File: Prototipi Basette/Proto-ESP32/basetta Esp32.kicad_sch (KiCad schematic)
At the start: 12 parts, among them J1 Conn_01x19, J2 Conn_01x19, J3 Conn_01x19, J4 Conn_01x19, J5 Screw_Terminal_01x02, J6 Conn_01x05, U1 L7805

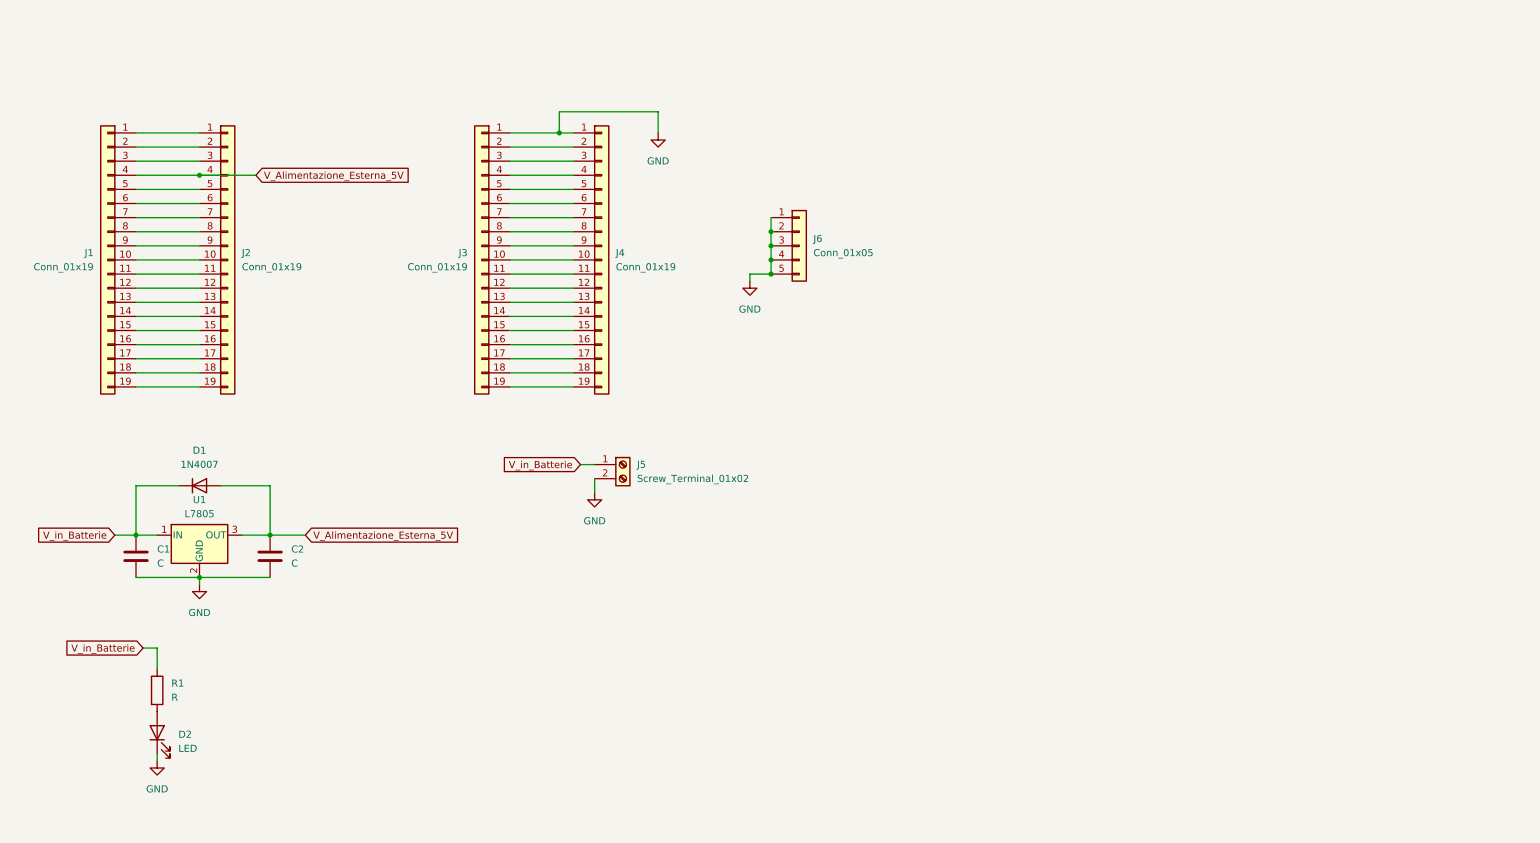
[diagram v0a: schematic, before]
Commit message: Add LM2596 symbol/footprint and update PCB
Add LM2596 footprint and symbol libraries, update project schematic and PCB files, and refresh project metadata. Includes new Library.pretty/LM2596 - IC footprint, Simboli_Progetto.* symbol library files, updated basetta Esp32.kicad_pcb/.kicad_sch/.kicad_pro/.kicad_prl and fp-info-cache, plus fp-lib-table and sym-lib-table. Several backup ZIPs were removed and replaced with new timestamped backups, and freerouting/temp freerouting files and a freerouting plugin ZIP were added.
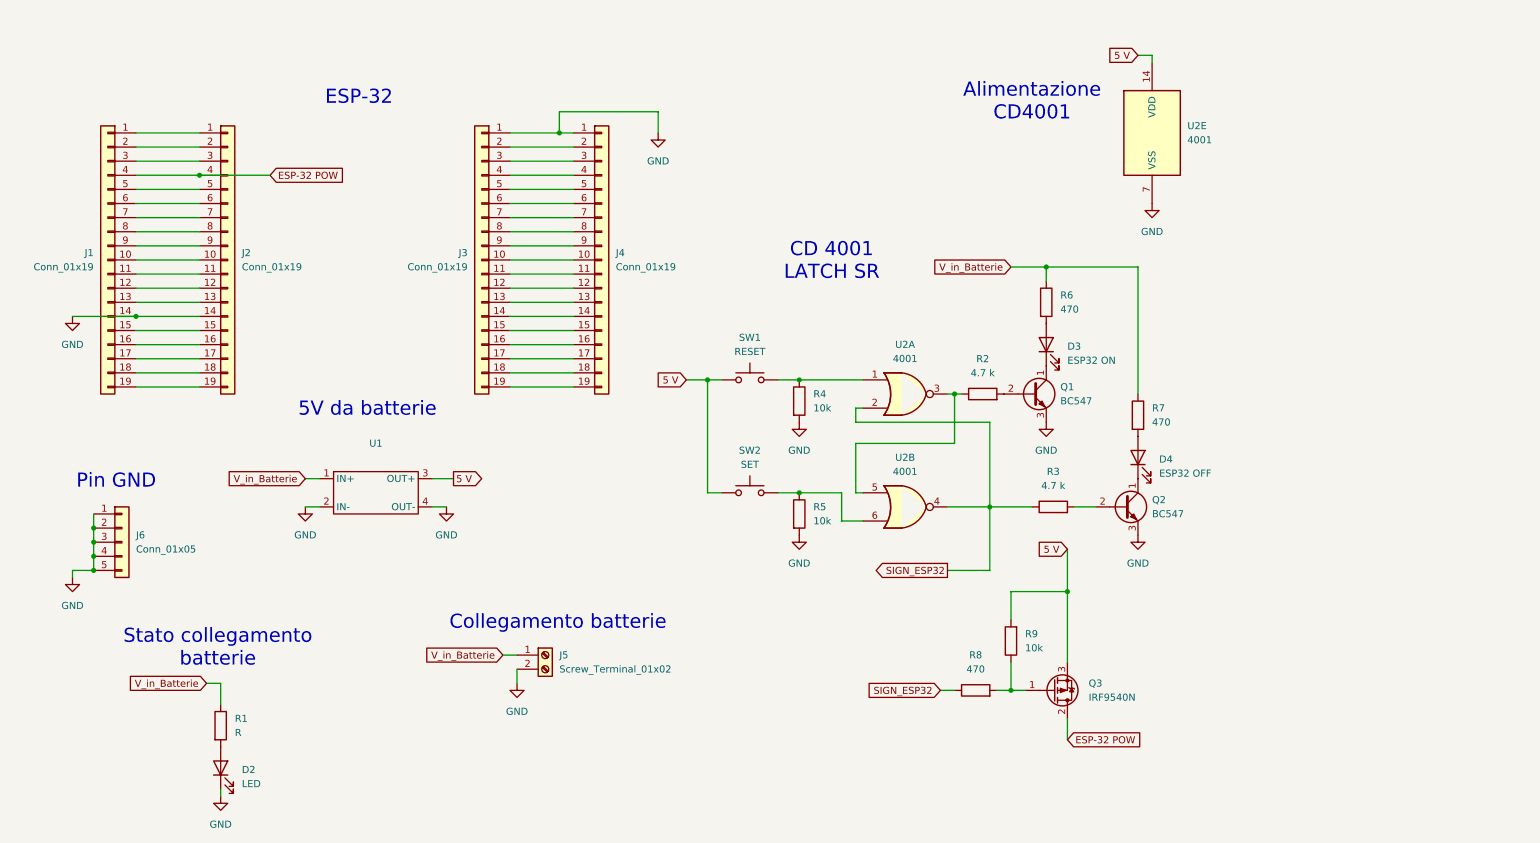
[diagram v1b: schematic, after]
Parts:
- removed C1: C, Capacitor_THT:C_Rect_L13.0mm_W5.0mm_P10.00mm_FKS3_FKP3_MKS4, symbol Device:C
- removed C2: C, Capacitor_THT:C_Disc_D5.0mm_W2.5mm_P5.00mm, symbol Device:C
- removed D1: 1N4007, Diode_THT:D_DO-41_SOD81_P7.62mm_Horizontal, symbol Diode:1N4007
- removed U1: L7805, Package_TO_SOT_THT:TO-220-3_Horizontal_TabUp, symbol Regulator_Linear:L7805
- added D3: ESP32 ON, LED_THT:LED_D5.0mm, symbol Device:LED
- added D4: ESP32 OFF, LED_THT:LED_D5.0mm, symbol Device:LED
- added Q1, Q2: BC547, Package_TO_SOT_THT:TO-92_Inline, symbol Transistor_BJT:BC547
- added Q3: IRF9540N, Package_TO_SOT_THT:TO-220-3_Vertical, symbol Transistor_FET:IRF9540N
- added R2, R3: 4.7 k, Resistor_THT:R_Axial_DIN0207_L6.3mm_D2.5mm_P7.62mm_Horizontal, symbol Device:R
- added R4, R5, R9: 10k, Resistor_THT:R_Axial_DIN0207_L6.3mm_D2.5mm_P7.62mm_Horizontal, symbol Device:R
- added R6, R7, R8: 470, Resistor_THT:R_Axial_DIN0207_L6.3mm_D2.5mm_P7.62mm_Horizontal, symbol Device:R
- added SW1: RESET, Button_Switch_THT:SW_PUSH_6mm_H4.3mm, symbol Switch:SW_Push
- added SW2: SET, Button_Switch_THT:SW_PUSH_6mm_H4.3mm, symbol Switch:SW_Push
- added U1: ~, Library:LM2596 - IC, symbol Simboli_Progetto:LM2596_IC
- added U2: 4001, Package_DIP:DIP-14_W7.62mm, symbol 4xxx:4001
- J5: footprint TerminalBlock:TerminalBlock_Altech_AK300-2_P5.00mm -> TerminalBlock:TerminalBlock_MaiXu_MX126-5.0-02P_1x02_P5.00mm
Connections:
- net GND: now also J1.14 (Pin_14), J2.14 (Pin_14), Q1.3 (E), Q2.3 (E), R4.2, R5.2, U1.2 (IN-), U1.4 (OUT-), U2.7 (VSS)
- net V_in_Batterie: now also R6.1, R7.1, U1.1 (IN+)
- net V_Alimentazione_Esterna_5V renamed ESP-32 POW
- net ESP-32 POW: now also Q3.2 (D)
- new net: R5.1, SW2.2, U2.6
- new net: Q2.2 (B), R3.2
- new net: D4.1 (K), Q2.1 (C)
- new net: Q3.1 (G), R8.2, R9.1
- new net: D4.2 (A), R7.2
- new net: R2.1, U2.3, U2.5
- new net: Q1.2 (B), R2.2
- new net: D3.2 (A), R6.2
- new net: R4.1, SW1.2, U2.1
- new net: D3.1 (K), Q1.1 (C)
- new net 5 V: Q3.3 (S), R9.2, SW1.1, SW2.1, U1.3 (OUT+), U2.14 (VDD)
- new net SIGN_ESP32: R3.1, R8.1, U2.2, U2.4
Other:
- note added: "5V da batterie"
- note added: "Alimentazione CD4001"
- note added: "CD 4001 LATCH SR"
- note added: "Collegamento batterie"
- note added: "ESP-32"
- note added: "Pin GND"
- note added: "Stato collegamento batterie"
- company: (none) -> Prof. Bernardis Pierluigi
- title: (none) -> Proto ESP-32
- moved on the sheet: D2, J5, J6, R1

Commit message: Update ESP32 board files and docs
Add compiled Arduino/main.pdf and simplify Arduino/pulsante.tex (remove blocking debouncing example and tidy Bounce2 section). Add several timestamped basetta Esp32 backup ZIPs. Large KiCad changes to basetta Esp32: update .kicad_pcb footprints, pads, nets and 3D models (replace/adjust LED/resistor footprints, add 1x19 pin socket connector, LM2596 module, DIP U3 and many pads; adjust silk/fab layers, pad geometry and UUIDs), and update related project files (.kicad_sch, .kicad_prl, freerouting.dsn and temp-freerouting.dsn). These changes refine the schematic/PCB layout and capture incremental backups.
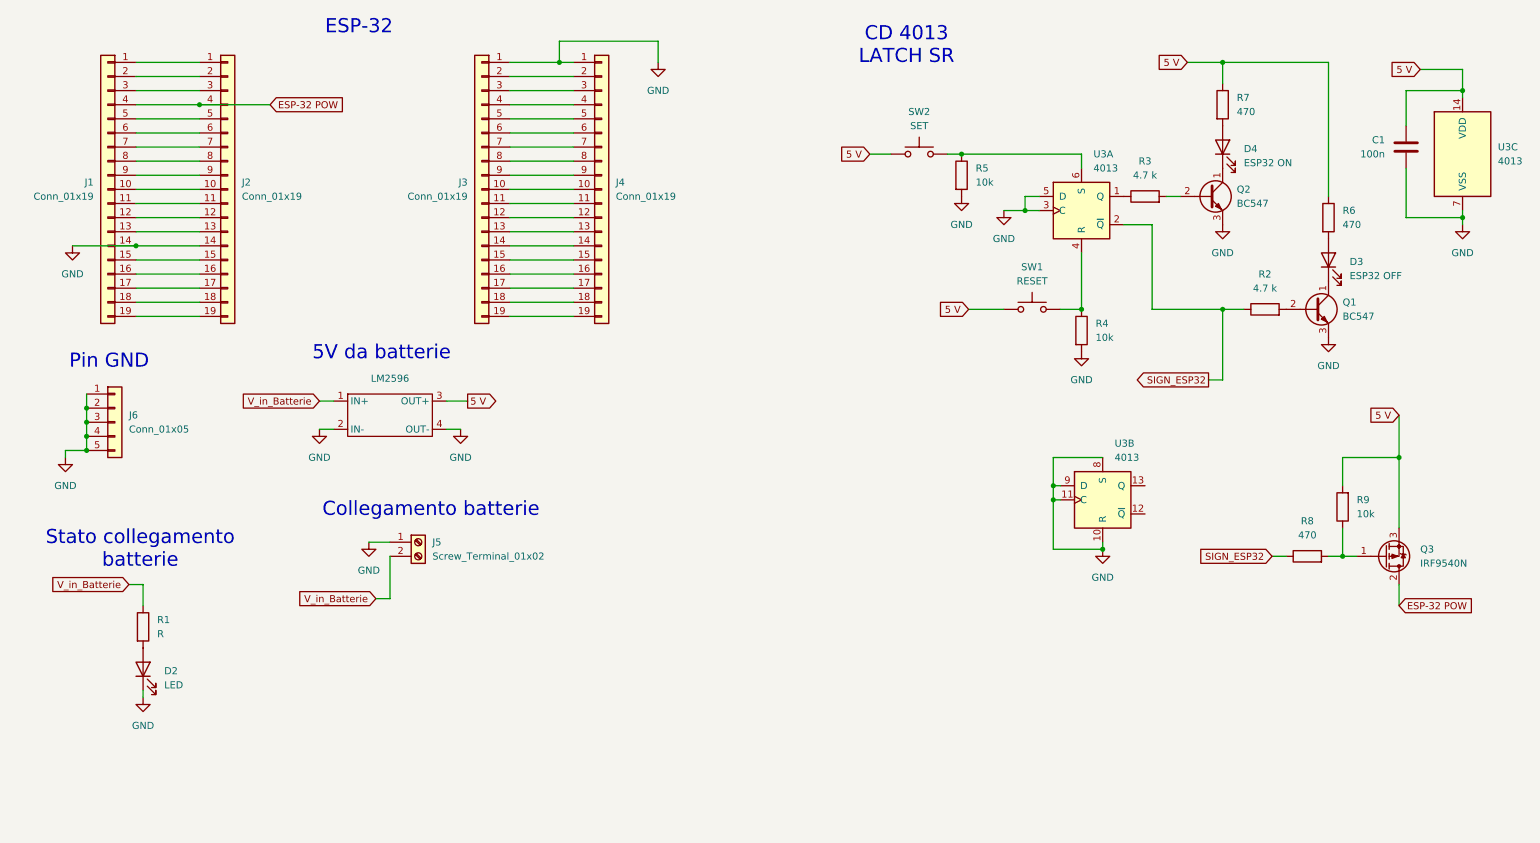
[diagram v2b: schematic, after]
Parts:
- removed U2: 4001, Package_DIP:DIP-14_W7.62mm, symbol 4xxx:4001
- added C1: 100n, Capacitor_THT:C_Disc_D5.0mm_W2.5mm_P5.00mm, symbol Device:C
- added U3: 4013, Package_DIP:DIP-14_W7.62mm_LongPads, symbol 4xxx:4013
- D3: value ESP32 ON -> ESP32 OFF
- D4: value ESP32 OFF -> ESP32 ON
- renumbered U1 to LM2596
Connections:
- net 5 V: now also R6.1, R7.1, C1.1, U3.14 (VDD)
- net GND: now also J5.1 (Pin_1), C1.2, U3.10 (R), U3.11 (C), U3.3 (C), U3.5 (D), U3.7 (VSS), U3.8 (S), U3.9 (D); no longer J5.2 (Pin_2)
- net SIGN_ESP32: now also R2.1, U3.2 (~{Q}); no longer R3.1
- net V_in_Batterie: now also J5.2 (Pin_2); no longer J5.1 (Pin_1), R6.1, R7.1
- net at R5.1, SW2.2: now also U3.6 (S)
- net at R4.1, SW1.2: now also U3.4 (R)
- new net: R3.1, U3.1 (Q)
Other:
- note added: "CD 4013 LATCH SR"
- note removed: "Alimentazione CD4001"
- note removed: "CD 4001 LATCH SR"
- moved on the sheet: D2, D3, D4, J1, J2, J3, J4, J5, J6, LM2596, Q1, Q2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

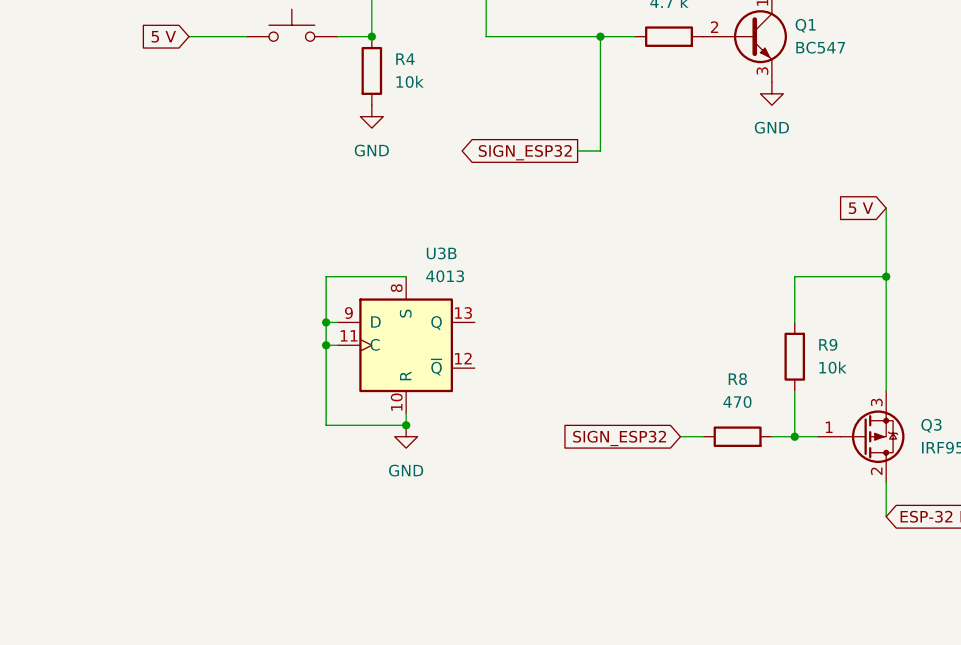
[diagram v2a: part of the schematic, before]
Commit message: Update KiCad PCB to newer format and footprints
Upgrade basetta Esp32.kicad_pcb to a newer pcbnew/generator version and apply footprint/pad updates. Changes include generator/version bump, expanded setup entries (tenting/covering/plugging), conversion of numeric net ids to named nets, normalized pinfunction names (suffixes added), adjusted footprint positions/orientations and many UUID updates, added unit definitions and duplicate_pad_numbers_are_jumpers flags, and cleaned Datasheet fields. Also add a timestamped backup zip of the project.
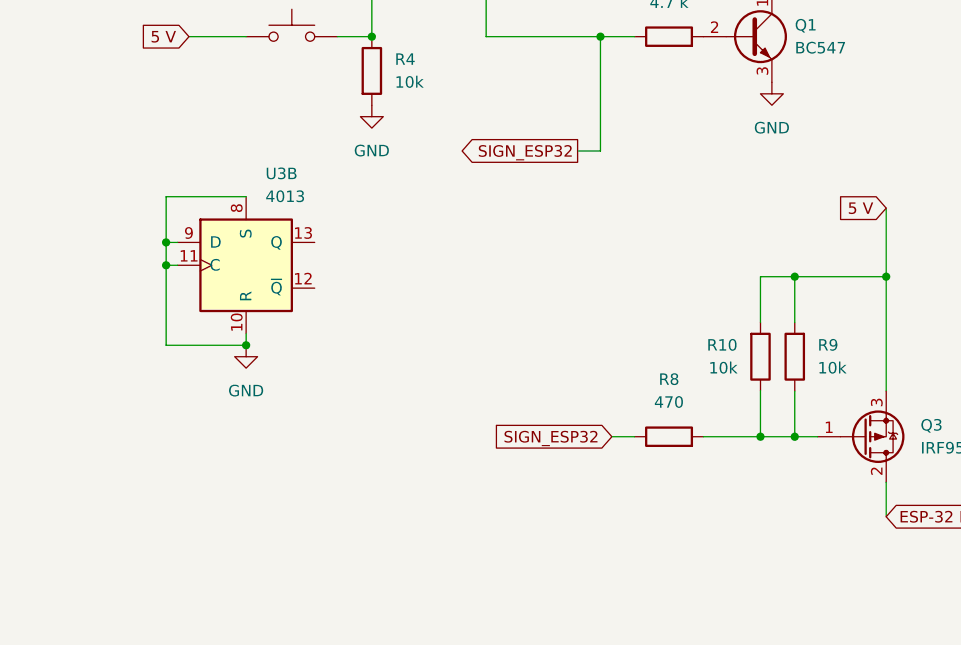
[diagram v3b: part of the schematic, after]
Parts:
- added R10: 10k, Resistor_THT:R_Axial_DIN0207_L6.3mm_D2.5mm_P7.62mm_Horizontal, symbol Device:R
- LM2596: value ~ -> (none)
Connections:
- net 5 V: now also R10.2
- net at Q3.1 (G), R8.2, R9.1: now also R10.1
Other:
- moved on the sheet: R8, U3B

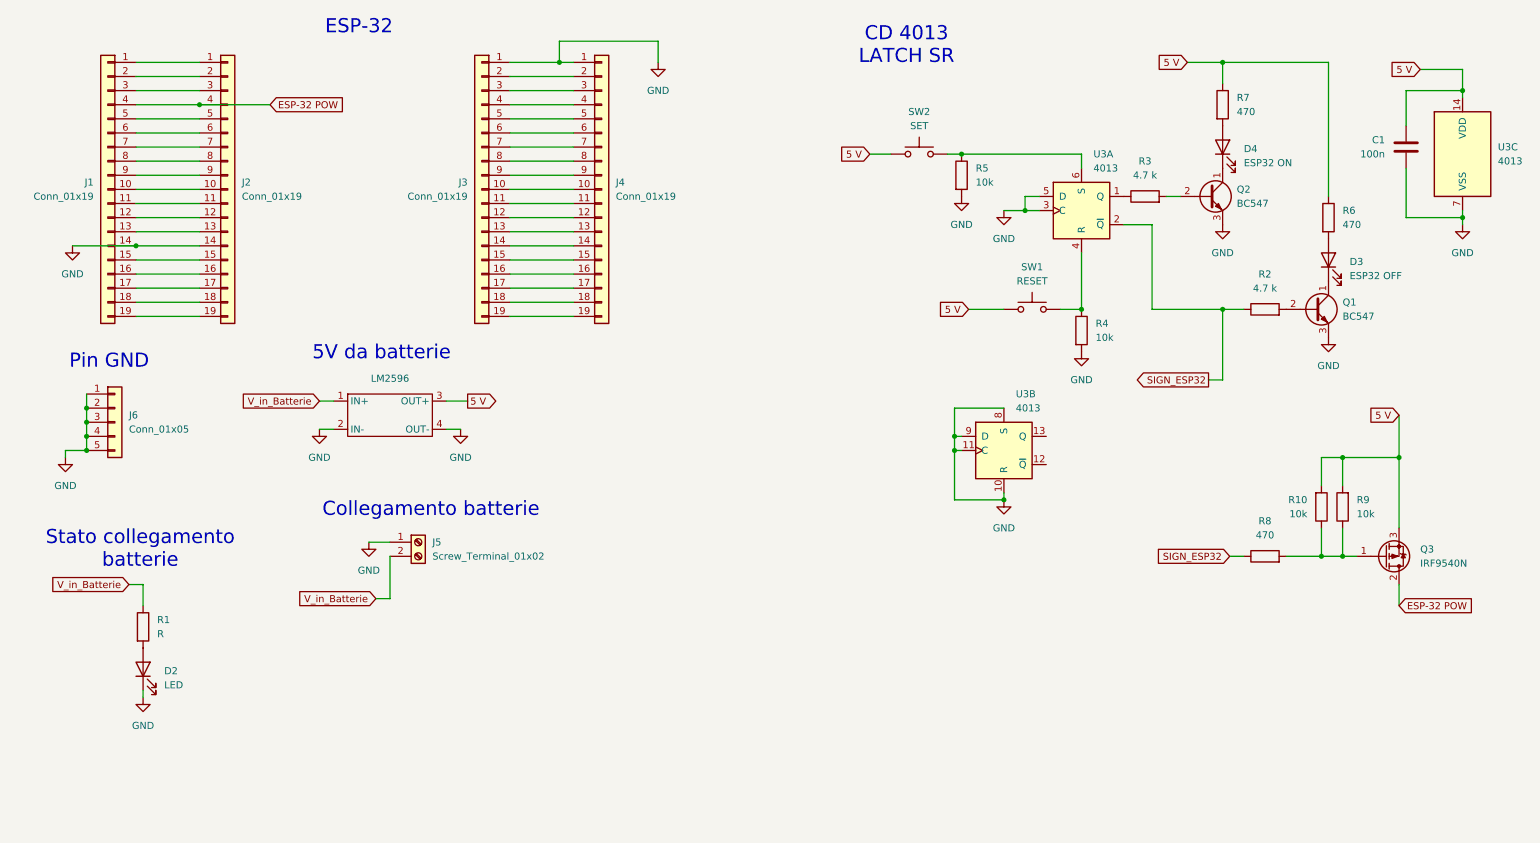
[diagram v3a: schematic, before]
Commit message: Modifica PCB - Parallelo Suicide
Aggiunto comando suicide da ESP32
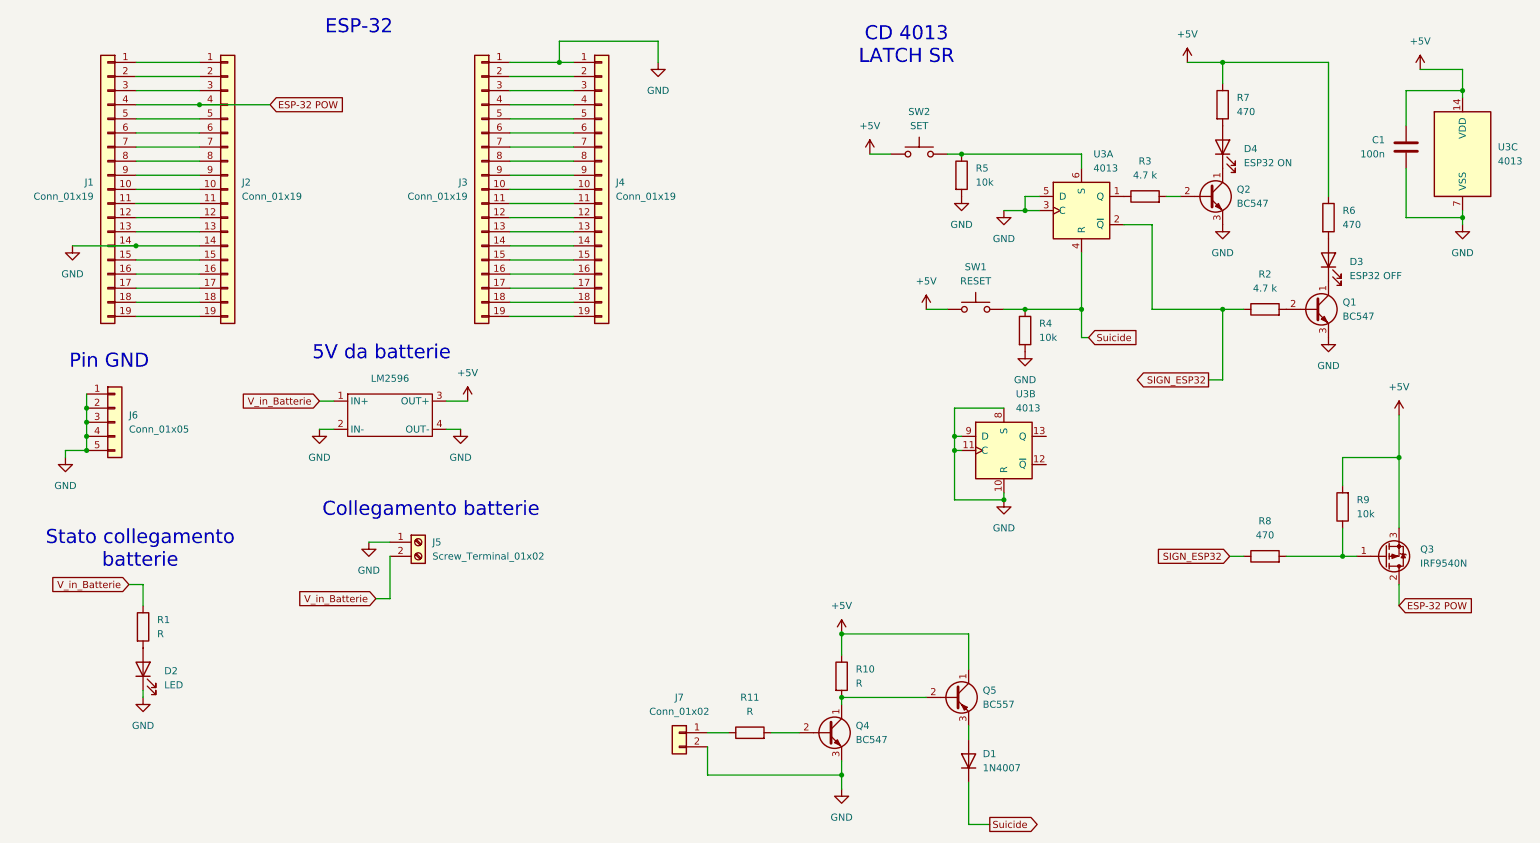
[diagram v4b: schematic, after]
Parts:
- added D1: 1N4007, Diode_THT:D_DO-41_SOD81_P7.62mm_Horizontal, symbol Diode:1N4007
- added J7: Conn_01x02, Connector_PinHeader_2.54mm:PinHeader_1x02_P2.54mm_Vertical, symbol Connector_Generic:Conn_01x02
- added Q4: BC547, Package_TO_SOT_THT:TO-92_Inline, symbol Transistor_BJT:BC547
- added Q5: BC557, Package_TO_SOT_THT:TO-92_Inline, symbol Transistor_BJT:BC557
- added R11: R, Resistor_THT:R_Axial_DIN0207_L6.3mm_D2.5mm_P7.62mm_Horizontal, symbol Device:R
- R10: value 10k -> R
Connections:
- net GND: now also J7.2 (Pin_2), Q4.3 (E)
- net Suicide: now reaches R4.1, SW1.2, U3.4 (R)
- net Suicide: now also D1.1 (K)
- net at Q3.1 (G), R8.2, R9.1: no longer R10.1
- net 5 V renamed +5V
- net +5V: now also R10.1, Q5.1 (C); no longer R10.2
- new net: J7.1 (Pin_1), R11.1
- new net: Q4.2 (B), R11.2
- new net: Q4.1 (C), Q5.2 (B), R10.2
- new net: D1.2 (A), Q5.3 (E)
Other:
- moved on the sheet: R4, SW1
